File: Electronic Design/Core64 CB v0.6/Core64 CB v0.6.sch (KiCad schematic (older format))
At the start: 20 parts, among them J1 929834-04-36-RK, J2 929834-04-36-RK, U1 SI7210-B-01, U2 SI7210-B-02, U3 SI7210-B-03, U4 SI7210-B-04, U5 RPR-0521RS

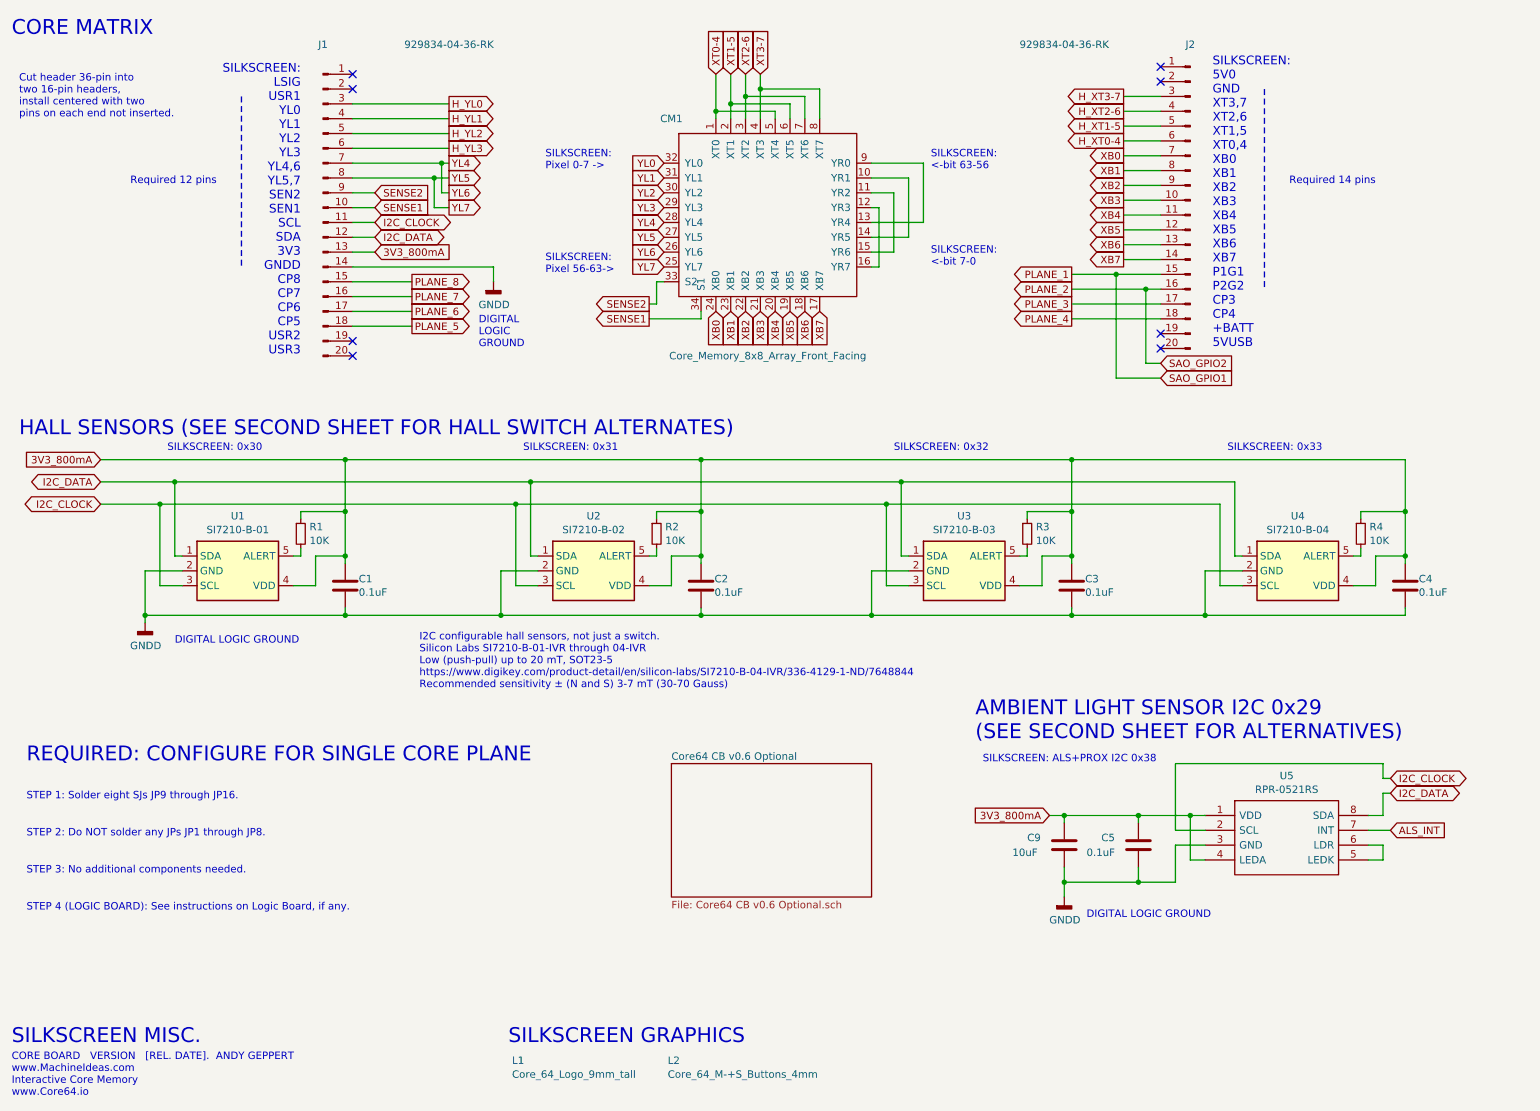
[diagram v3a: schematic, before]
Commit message: CB V0.6 added ALS and PROX, removed bottom ALS, complete BOM, PNP, and Gerbers for fabrication
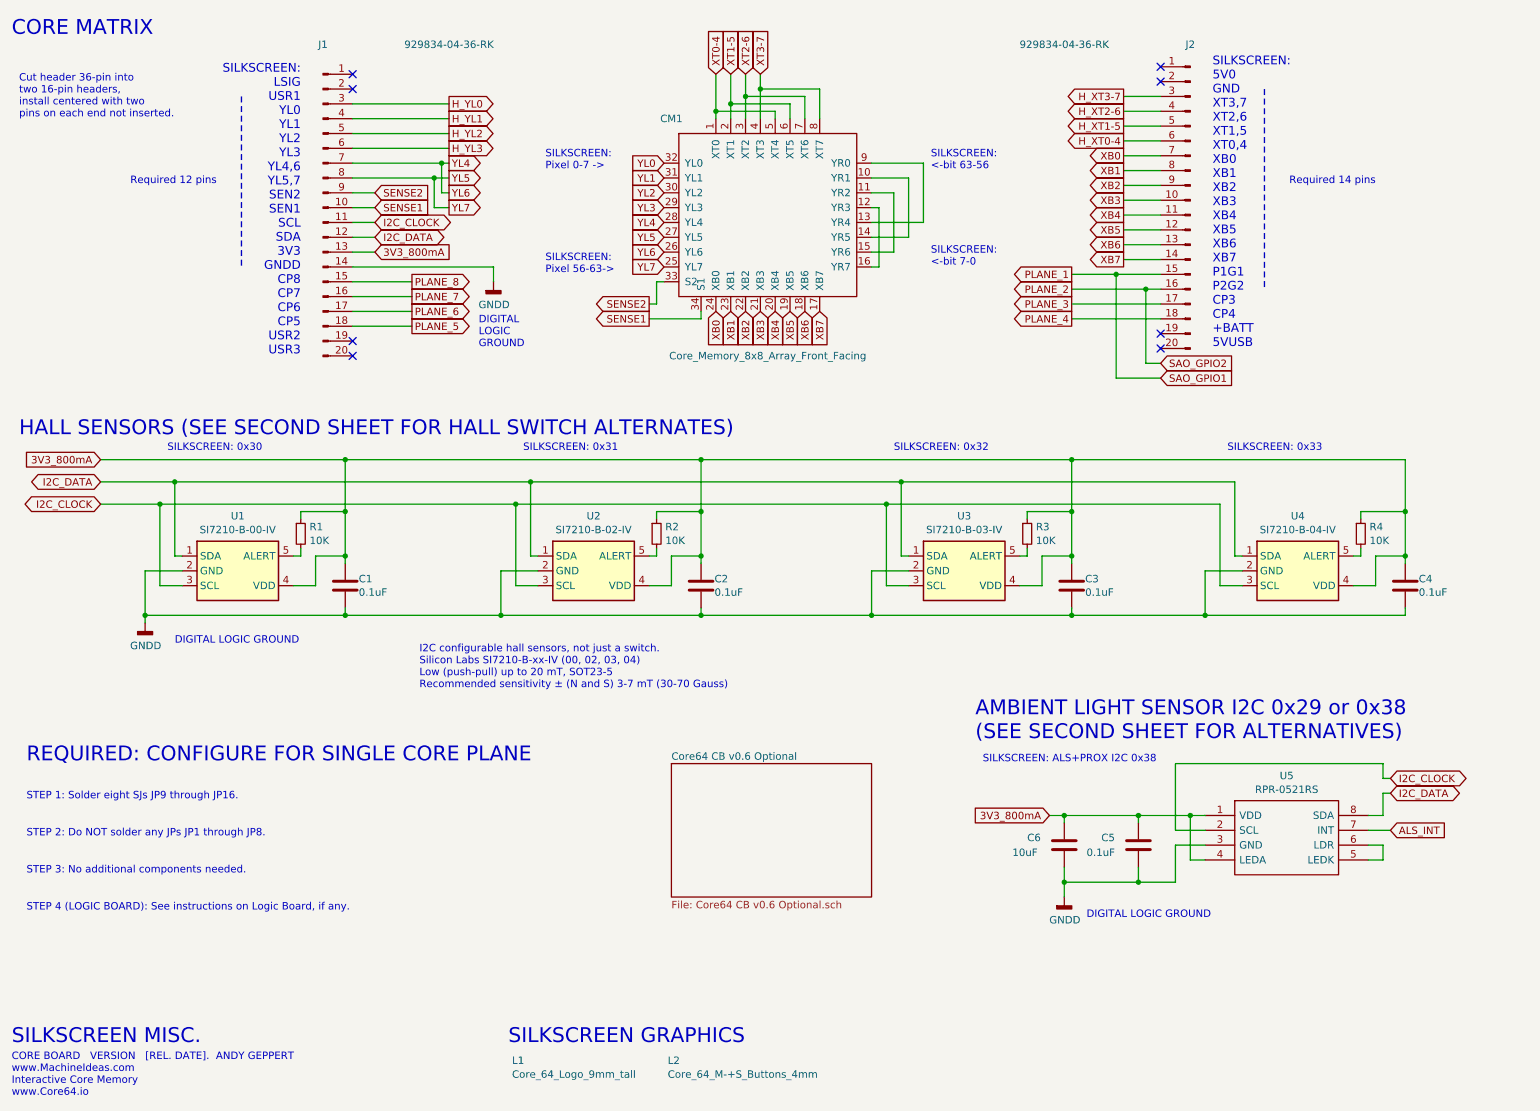
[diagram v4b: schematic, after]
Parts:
- C1, C2, C3, C4: Description (none) -> Capacitor; Insert (none) -> YES; Value_Modifer (none) -> X7R ceramic
- C5: Description (none) -> Capacitor; Insert (none) -> NO; Value_Modifer (none) -> X7R ceramic
- C6: renamed from C9; Description (none) -> Capacitor; Insert (none) -> NO; Value_Modifer (none) -> X7R ceramic
- CM1: Description (none) -> Opening for the cores and wire grid; Insert (none) -> NO
- J1, J2: Insert (none) -> NO; Manufacturer 3M -> (none); Manufacturer_Name (none) -> 3M; Supplier (Primary) (none) -> Mouser; Supplier SKU (Primary) (none) -> 517-929834-04-36-RK
- L1, L2: Description (none) -> Silkscreen; Insert (none) -> NO
- R1, R2, R3, R4: Description (none) -> Resistor; Insert (none) -> YES; Value_Modifer (none) -> 10%
- U1: value SI7210-B-01 -> SI7210-B-00-IV; Alt. Manufacturer (none) -> None; Alt. Mfg P/N (none) -> None; Description (none) -> Si7210 Series I2C Hall Effect Magnetic Position and Tempera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; Insert (none) -> YES; Manufacturer_Name (none) -> Silicon Labs; Mfg P/N (none) -> SI7210-B-00-IV; Supplier (2nd) (none) -> Arrow; Supplier (Primary) (none) -> Newark; Supplier SKU (2nd) (none) -> si7210-b-00-iv; Supplier SKU (Primary) (none) -> 31AC1357
- U2: value SI7210-B-02 -> SI7210-B-02-IV; Alt. Manufacturer (none) -> None; Alt. Mfg P/N (none) -> None; Description (none) -> Si7210 Series I2C Hall Effect Magnetic Position and Tempera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; Insert (none) -> YES; Manufacturer_Name (none) -> Silicon Labs; Mfg P/N (none) -> SI7210-B-02-IV; Supplier (2nd) (none) -> Mouser; Supplier (Primary) (none) -> Newark; Supplier SKU (2nd) (none) -> 634-SI7210-B-02-IV; Supplier SKU (Primary) (none) -> 31AC1359
- U3: value SI7210-B-03 -> SI7210-B-03-IV; Alt. Manufacturer (none) -> None; Alt. Mfg P/N (none) -> None; Description (none) -> Si7210 Series I2C Hall Effect Magnetic Position and Tempera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; Insert (none) -> YES; Manufacturer_Name (none) -> Silicon Labs; Mfg P/N (none) -> SI7210-B-03-IV; Supplier (2nd) (none) -> Mouser; Supplier (Primary) (none) -> Newark; Supplier SKU (2nd) (none) -> 634-SI7210-B-03-IV; Supplier SKU (Primary) (none) -> 31AC1360
- U4: value SI7210-B-04 -> SI7210-B-04-IV; Alt. Manufacturer (none) -> None; Alt. Mfg P/N (none) -> None; Description (none) -> Si7210 Series I2C Hall Effect Magnetic Position and Tempera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; Insert (none) -> YES; Manufacturer_Name (none) -> Silicon Labs; Mfg P/N (none) -> SI7210-B-04-IV; Supplier (2nd) (none) -> Arrow; Supplier (Primary) (none) -> Mouser; Supplier SKU (2nd) (none) -> si7210-b-04-iv; Supplier SKU (Primary) (none) -> 634-SI7210-B-04-IV
- U5: Alt. Manufacturer (none) -> None; Alt. Mfg P/N (none) -> None; Description ALS w/prx 1.8V logic w/ IrLED driver -> I2C Digital Light Sensor, ALS w/prox 1.8V logic w/IrLED dri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; Insert (none) -> NO; Mfg P/N (none) -> RPR-0521RS
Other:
- note added: "AMBIENT LIGHT SENSOR I2C 0x29 or 0x38\n(SEE SECOND SHEET FOR ALTERNATIVES)"
- note added: "I2C configurable hall sensors, not just a switch.\nSilicon Labs SI7210-B-xx-IV (00, 02, 03, 04)\nLow (push-pull) up to 20 mT, SOT23-5\nRecommended sensitivity ± (N and S) 3-7 mT (30-70 Gauss)"
- note removed: "AMBIENT LIGHT SENSOR I2C 0x29\n(SEE SECOND SHEET FOR ALTERNATIVES)"
- note removed: "I2C configurable hall sensors, not just a switch.\nSilicon Labs SI7210-B-01-IVR through 04-IVR\nLow (push-pull) up to 20 mT, SOT23-5\nhttps://www.digikey.com/product-detail/en/silicon-labs/SI7210-B-04-IVR/336-4129-1-ND/7648844\nRecommended sensitivity ± (N and S) 3-7 mT (30-70 Gauss)"
